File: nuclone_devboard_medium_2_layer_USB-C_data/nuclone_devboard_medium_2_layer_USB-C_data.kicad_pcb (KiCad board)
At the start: 2 copper layers, 50 x 76.2 mm, 40 parts, among them J1 JTAG_2X05, J2 TYPE-C-31-M-12, J3 nuclone_medium_left, J4 nuclone_medium_right, J5 Conn_02x06_Odd_Even, SW1 RESET, SW2 Bootloader, U1 MCP1702-3.3V, U2 TPESD0504C6

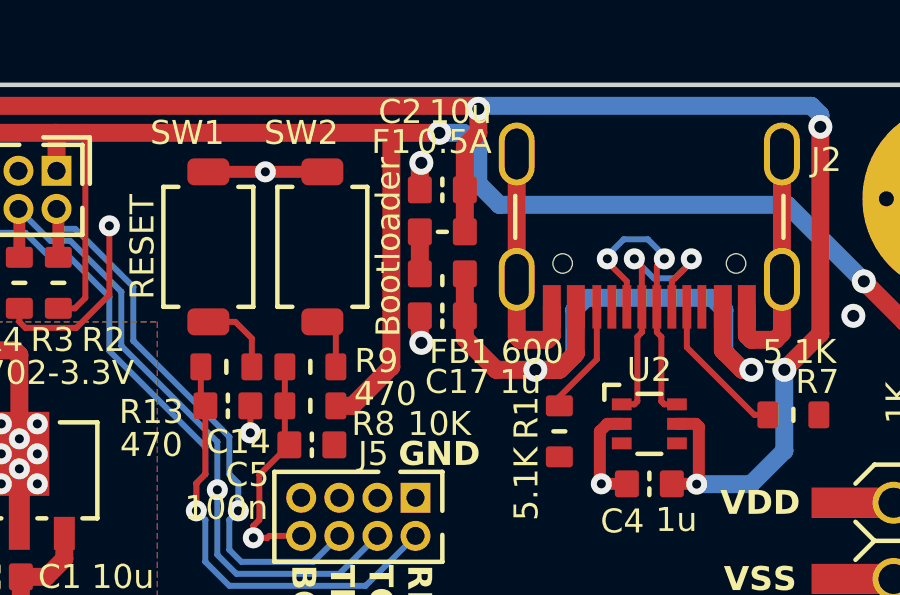
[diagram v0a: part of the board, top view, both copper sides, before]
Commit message: added diode, updated library
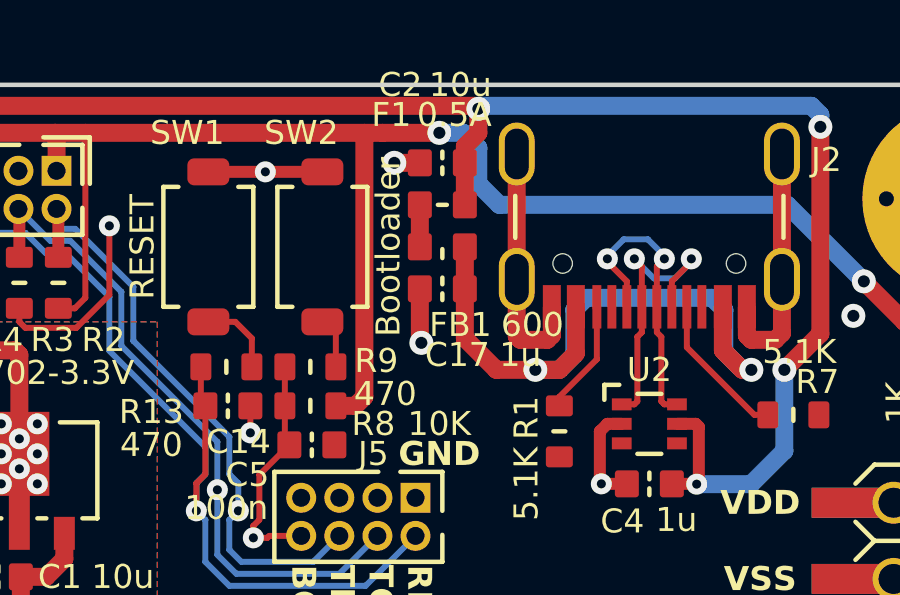
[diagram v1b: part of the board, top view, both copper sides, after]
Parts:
- moved C17 0.90 mm to (89.1, 67.8)
- moved F1 0.90 mm to (89.1, 65.0)
- moved C2 0.90 mm to (89.1, 63.6)
- moved FB1 0.90 mm to (89.1, 66.4)
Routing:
- net /VBUS: track 91.2 -> 90.3 mm
- net Net-(C17-Pad2): track 21.6 -> 22.5 mm
- net /VSS: track 44.6 -> 45.5 mm
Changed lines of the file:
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@@
   )
   (footprint "SquantorCapacitor:C_0603" (layer "F.Cu")
-    (at 89.1 64.5)
+    (at 89.1 63.6)
     (descr "Capacitor SMD 0603, reflow soldering, AVX (see smccp.pdf)")
     (tags "capacitor 0603")
@@
   )
   (footprint "SquantorFuse:F_0603_hand" (layer "F.Cu")
-    (at 89.1 65.9 180)
+    (at 89.1 65 180)
     (descr "Fuse SMD 0603, reflow soldering")
     (tags "fuse 0603")
@@
   )
   (footprint "SquantorInductor:L_0603" (layer "F.Cu")
-    (at 89.1 67.3)
+    (at 89.1 66.4)
     (descr "Inductor SMD 0603")
     (tags "Inductor 0402")
@@
   )
   (footprint "SquantorCapacitor:C_0603" (layer "F.Cu")
-    (at 89.1 68.7)
+    (at 89.1 67.8)
     (descr "Capacitor SMD 0603, reflow soldering, AVX (see smccp.pdf)")
     (tags "capacitor 0603")
@@
   (segment (start 67.8 63.6) (end 69.7 61.7) (width 0.6) (layer "F.Cu") (net 1))
   (segment (start 97.566774 74.3) (end 96.75 74.3) (width 0.4) (layer "F.Cu") (net 1))
-  (segment (start 90.3 62.6) (end 89.85 63.05) (width 0.6) (layer "F.Cu") (net 1))
-  (segment (start 89.85 64.5) (end 89.85 65.9) (width 0.6) (layer "F.Cu") (net 1))
   (segment (start 74.4 73.3) (end 75 73.8) (width 0.6) (layer "F.Cu") (net 1))
   (segment (start 101.7 69.3) (end 101.7 62.4) (width 0.6) (layer "F.Cu") (net 1))
   (segment (start 74.9 72.8) (end 75 72.8) (width 0.6) (layer "F.Cu") (net 1))
+  (segment (start 89.85 63.6) (end 89.85 65) (width 0.6) (layer "F.Cu") (net 1))
   (segment (start 75 72.9) (end 75 72.9) (width 0.6) (layer "F.Cu") (net 1))
   (segment (start 97.577735 74.310961) (end 97.65 74.238696) (width 0.4) (layer "F.Cu") (net 1))
-  (segment (start 90.3 61.8) (end 90.3 62.6) (width 0.6) (layer "F.Cu") (net 1))
   (segment (start 74.85 69.85) (end 75 70) (width 0.6) (layer "F.Cu") (net 1))
+  (segment (start 90.3 62.6) (end 89.85 63.05) (width 0.6) (layer "F.Cu") (net 1))
   (segment (start 69.7 69.85) (end 74.85 69.85) (width 0.6) (layer "F.Cu") (net 1))
   (segment (start 97.65 72.4) (end 97.55 72.3) (width 0.4) (layer "F.Cu") (net 1))
   (segment (start 75 70) (end 75 72.8) (width 0.6) (layer "F.Cu") (net 1))
-  (segment (start 89.85 63.05) (end 89.85 64.5) (width 0.6) (layer "F.Cu") (net 1))
+  (segment (start 90.3 61.8) (end 90.3 62.6) (width 0.6) (layer "F.Cu") (net 1))
   (segment (start 97.577735 74.310961) (end 97.566774 74.3) (width 0.4) (layer "F.Cu") (net 1))
   (segment (start 75 72.9) (end 74.4 73.3) (width 0.6) (layer "F.Cu") (net 1))
@@
   (segment (start 67.7 68.9) (end 67.8 68.8) (width 0.6) (layer "F.Cu") (net 1))
   (segment (start 69.7 68.9) (end 69.7 69.85) (width 0.6) (layer "F.Cu") (net 1))
+  (segment (start 89.85 63.05) (end 89.85 63.6) (width 0.6) (layer "F.Cu") (net 1))
   (segment (start 97.55 72.3) (end 96.92 72.3) (width 0.4) (layer "F.Cu") (net 1))
   (via (at 97.577735 74.310961) (size 0.7) (drill 0.3) (layers "F.Cu" "B.Cu") (net 1))
@@
   (segment (start 67.03 77.47) (end 66.04 77.47) (width 0.6) (layer "B.Cu") (net 1))
   (segment (start 67.1 77.4) (end 67.03 77.47) (width 0.6) (layer "B.Cu") (net 1))
-  (segment (start 88.35 67.3) (end 88.35 65.9) (width 0.6) (layer "F.Cu") (net 2))
+  (segment (start 88.35 66.4) (end 88.35 65) (width 0.6) (layer "F.Cu") (net 2))
   (segment (start 68.9 68.1) (end 70.2 68.1) (width 0.2) (layer "F.Cu") (net 3))
-  (segment (start 86.1 71.7) (end 85.55 71.7) (width 0.6) (layer "F.Cu") (net 3))
   (segment (start 76.5 76.8) (end 75.9 77.4) (width 0.6) (layer "F.Cu") (net 3))
   (segment (start 76.85 68.45) (end 77.2 68.1) (width 0.2) (layer "F.Cu") (net 3))
@@
   (segment (start 68.7 64) (end 70.1 62.6) (width 0.6) (layer "F.Cu") (net 3))
   (segment (start 68.7 67.9) (end 68.7 64) (width 0.6) (layer "F.Cu") (net 3))
+  (segment (start 86.5 62.6) (end 86.5 71.4) (width 0.6) (layer "F.Cu") (net 3))
   (segment (start 70.1 62.6) (end 76.2 62.6) (width 0.6) (layer "F.Cu") (net 3))
   (segment (start 108.97 74.93) (end 109 74.9) (width 0.6) (layer "F.Cu") (net 3))
@@
   (segment (start 68.7 67.9) (end 68.7 70.3) (width 0.6) (layer "F.Cu") (net 3))
   (segment (start 89 62.6) (end 87.1 62.6) (width 0.6) (layer "F.Cu") (net 3))
-  (segment (start 87.4 62.6) (end 87.4 70.4) (width 0.6) (layer "F.Cu") (net 3))
   (segment (start 76.24 62.64) (end 76.2 62.6) (width 0.6) (layer "F.Cu") (net 3))
   (segment (start 70.55 68.45) (end 71.1 68.45) (width 0.2) (layer "F.Cu") (net 3))
@@
   (segment (start 67.8 71.2) (end 67.8 74.93) (width 0.6) (layer "F.Cu") (net 3))
   (segment (start 75.05 78.35) (end 75 78.4) (width 0.6) (layer "F.Cu") (net 3))
-  (segment (start 87.4 70.4) (end 86.1 71.7) (width 0.6) (layer "F.Cu") (net 3))
   (segment (start 69.03 74.93) (end 67.12 74.93) (width 0.6) (layer "F.Cu") (net 3))
   (segment (start 108.9 68.9) (end 104.5 68.9) (width 0.6) (layer "F.Cu") (net 3))
+  (segment (start 86.5 71.4) (end 86.2 71.7) (width 0.6) (layer "F.Cu") (net 3))
+  (segment (start 86.2 71.7) (end 85.55 71.7) (width 0.6) (layer "F.Cu") (net 3))
   (segment (start 109 73.8) (end 109.2 73.6) (width 0.6) (layer "F.Cu") (net 3))
   (segment (start 75.05 77.4) (end 75.05 78.35) (width 0.6) (layer "F.Cu") (net 3))
@@
   (segment (start 92.6 69.5) (end 91.7 69.5) (width 0.6) (layer "F.Cu") (net 4))
   (segment (start 84.7 63.9) (end 83.2 63.9) (width 0.4) (layer "F.Cu") (net 4))
-  (segment (start 88.35 68.7) (end 88.35 69.55) (width 0.6) (layer "F.Cu") (net 4))
   (segment (start 94.4 74.3) (end 95.25 74.3) (width 0.4) (layer "F.Cu") (net 4))
-  (segment (start 88.35 69.55) (end 88.4 69.6) (width 0.6) (layer "F.Cu") (net 4))
   (segment (start 92.75 68.4) (end 92.75 69.35) (width 0.6) (layer "F.Cu") (net 4))
   (segment (start 100.2 69.5) (end 100.42 69.28) (width 0.6) (layer "F.Cu") (net 4))
@@
   (segment (start 75 68.9) (end 75.2 69.1) (width 0.2) (layer "F.Cu") (net 4))
   (segment (start 75.2 69.1) (end 76.9 69.1) (width 0.2) (layer "F.Cu") (net 4))
-  (segment (start 88.4 63.6) (end 88.35 63.65) (width 0.6) (layer "F.Cu") (net 4))
-  (segment (start 88.35 63.65) (end 88.35 64.5) (width 0.6) (layer "F.Cu") (net 4))
+  (segment (start 88.35 67.8) (end 88.35 69.55) (width 0.6) (layer "F.Cu") (net 4))
+  (segment (start 87.5 63.6) (end 88.35 63.6) (width 0.6) (layer "F.Cu") (net 4))
   (segment (start 100.42 63.305) (end 100.42 67.485) (width 0.6) (layer "F.Cu") (net 4))
   (segment (start 81.3 63.9) (end 83.2 63.9) (width 0.4) (layer "F.Cu") (net 4))
@@
   (segment (start 75 68.45) (end 75 68.9) (width 0.2) (layer "F.Cu") (net 4))
   (segment (start 76.9 69.1) (end 78 68) (width 0.2) (layer "F.Cu") (net 4))
+  (segment (start 88.35 69.55) (end 88.4 69.6) (width 0.6) (layer "F.Cu") (net 4))
   (segment (start 73.5 77.35) (end 73.55 77.4) (width 0.6) (layer "F.Cu") (net 4))
   (segment (start 91.58 69.38) (end 91.58 67.485) (width 0.6) (layer "F.Cu") (net 4))
@@
   (via (at 94.4 74.3) (size 0.7) (drill 0.3) (layers "F.Cu" "B.Cu") (net 4))
   (via (at 86.7 91) (size 0.7) (drill 0.3) (layers "F.Cu" "B.Cu") (free) (net 4))
-  (via (at 88.4 63.6) (size 0.8) (drill 0.4) (layers "F.Cu" "B.Cu") (net 4))
+  (via (at 87.5 63.6) (size 0.8) (drill 0.4) (layers "F.Cu" "B.Cu") (net 4))
   (via (at 66.6 61.8) (size 0.8) (drill 0.4) (layers "F.Cu" "B.Cu") (free) (net 4))
   (via (at 78 65.7) (size 0.7) (drill 0.3) (layers "F.Cu" "B.Cu") (net 4))
@@
   (segment (start 82.2 68.9) (end 82.75 69.45) (width 0.2) (layer "F.Cu") (net 19))
   (segment (start 92.2 70.5) (end 93 70.5) (width 0.6) (layer "F.Cu") (net 21))
-  (segment (start 92.2 70.5) (end 90.9 70.5) (width 0.6) (layer "F.Cu") (net 21))
-  (segment (start 89.85 68.7) (end 89.85 67.3) (width 0.6) (layer "F.Cu") (net 21))
+  (segment (start 90.9 70.5) (end 89.85 69.45) (width 0.6) (layer "F.Cu") (net 21))
   (segment (start 98.45 69.85) (end 98.45 68.4) (width 0.6) (layer "F.Cu") (net 21))
+  (segment (start 92.2 70.5) (end 90.9 70.5) (width 0.6) (layer "F.Cu") (net 21))
+  (segment (start 89.85 67.8) (end 89.85 66.4) (width 0.6) (layer "F.Cu") (net 21))
+  (segment (start 89.85 69.45) (end 89.85 67.8) (width 0.6) (layer "F.Cu") (net 21))
   (segment (start 93 70.5) (end 93.55 69.95) (width 0.6) (layer "F.Cu") (net 21))
   (segment (start 99.1 70.5) (end 98.45 69.85) (width 0.6) (layer "F.Cu") (net 21))
   (segment (start 99.4 70.5) (end 99.1 70.5) (width 0.6) (layer "F.Cu") (net 21))
-  (segment (start 89.85 69.45) (end 89.85 68.7) (width 0.6) (layer "F.Cu") (net 21))
   (segment (start 93.55 69.95) (end 93.55 68.4) (width 0.6) (layer "F.Cu") (net 21))
-  (segment (start 90.9 70.5) (end 89.85 69.45) (width 0.6) (layer "F.Cu") (net 21))
   (via (at 92.2 70.5) (size 0.8) (drill 0.4) (layers "F.Cu" "B.Cu") (net 21))
   (via (at 99.4 70.5) (size 0.8) (drill 0.4) (layers "F.Cu" "B.Cu") (net 21))

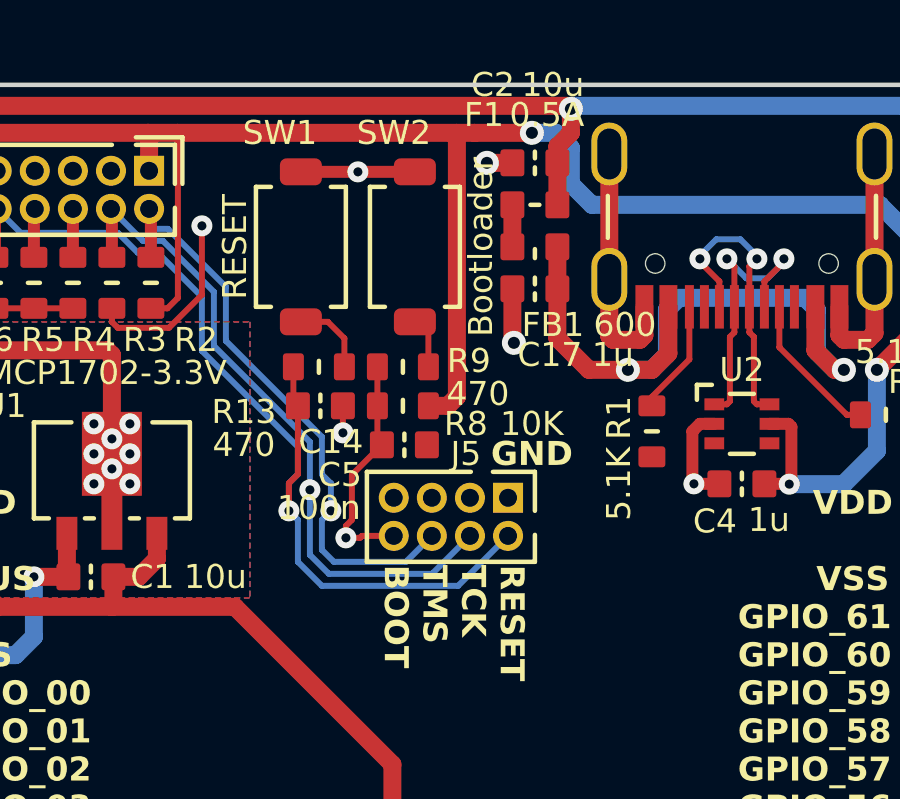
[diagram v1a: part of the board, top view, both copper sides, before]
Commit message: added diode in series
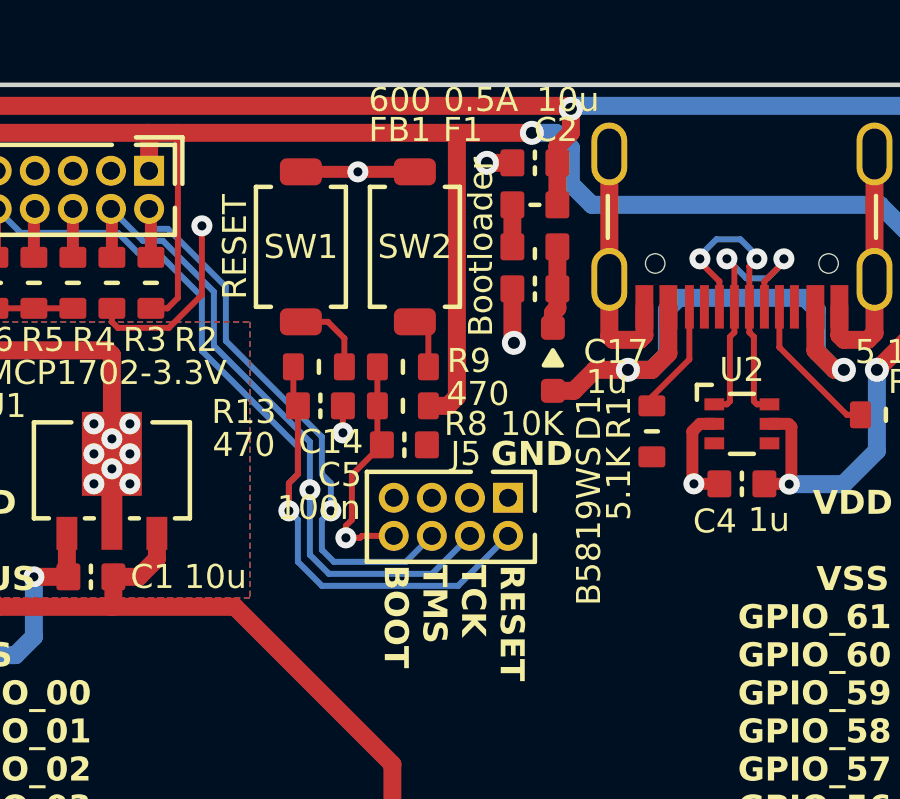
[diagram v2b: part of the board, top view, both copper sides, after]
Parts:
- added D1: B5819WS, SquantorDiodes:SOD-323-nexperia-hand, F.Cu at (89.7, 70.2)
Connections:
- net /Bootloader renamed /BOOT
- C17 pad 2: Net-(C17-Pad2) -> Net-(D1-K)
- FB1 pad 2: Net-(C17-Pad2) -> Net-(D1-K)
- J2 pad A4B9: Net-(C17-Pad2) -> Net-(D1-A)
- J2 pad B4A9: Net-(C17-Pad2) -> Net-(D1-A)
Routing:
- net Net-(C17-Pad2): track 22.5 -> 0.00 mm, vias 2 -> 0
- net Net-(D1-A): track 0.00 -> 19.5 mm, vias 0 -> 2
- net Net-(D1-K): track 0.00 -> 2.76 mm

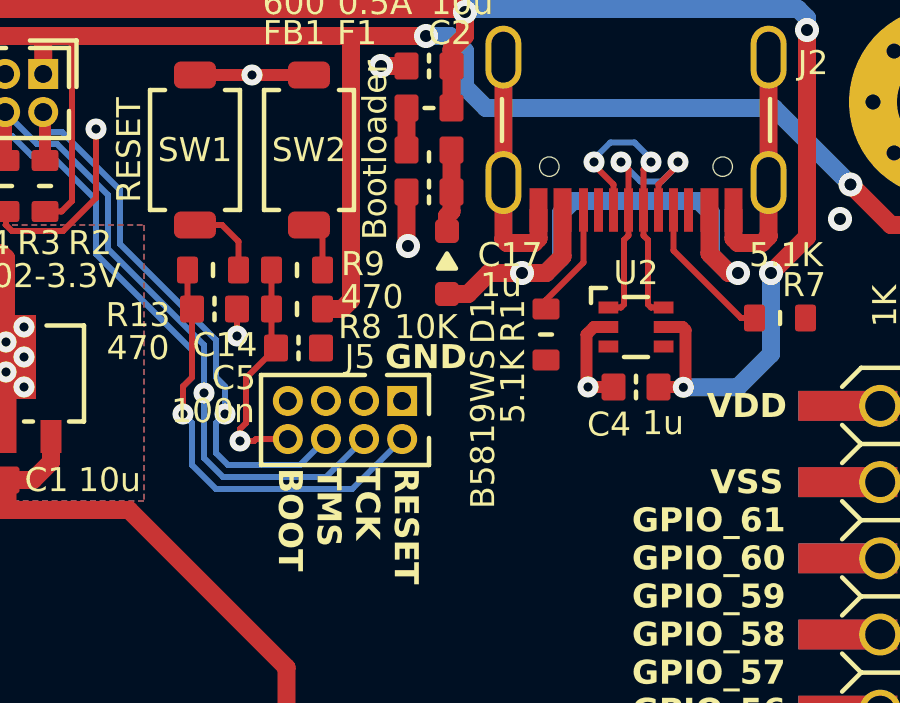
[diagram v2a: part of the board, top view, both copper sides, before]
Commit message: adjusted diode position a bit
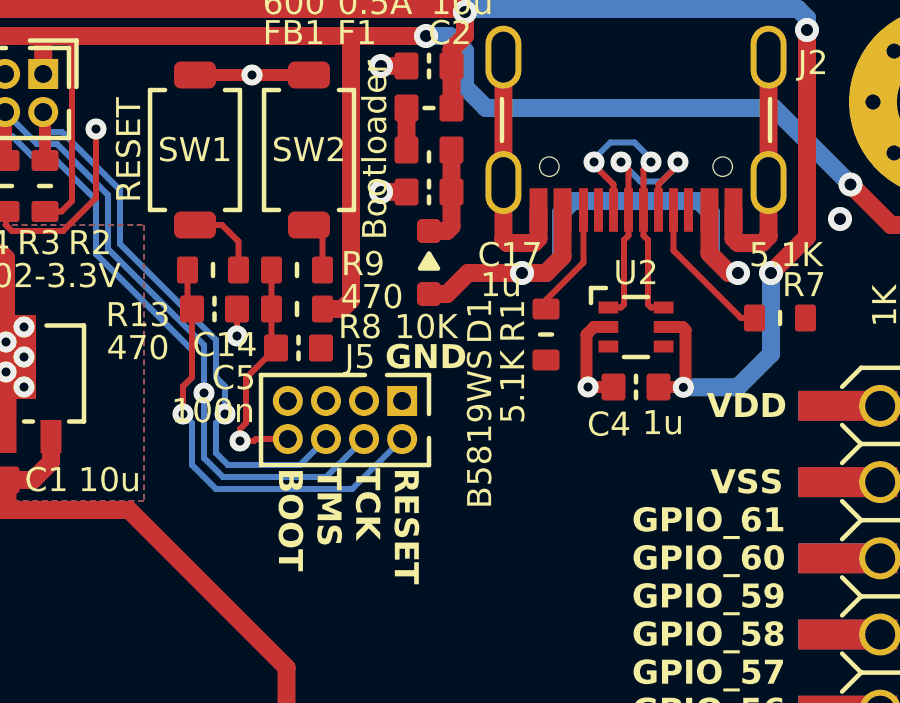
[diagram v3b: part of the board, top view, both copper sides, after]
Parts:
- moved D1 0.60 mm to (89.1, 70.2)
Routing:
- net /VSS: track 45.5 -> 44.5 mm
- net Net-(D1-K): track 2.76 -> 3.36 mm
- net Net-(D1-A): track 19.5 -> 20.1 mm
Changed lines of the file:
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@@
   )
   (footprint "SquantorDiodes:SOD-323-nexperia-hand" (layer "F.Cu")
-    (at 89.7 70.15 -90)
+    (at 89.1 70.15 -90)
     (descr "nexperia SOD-323 footprint hand soldering")
     (tags "SOD-323")
@@
     (property "ki_keywords" "diode")
     (attr smd)
-    (fp_text reference "D1" (at 1.95 -1.2 90 unlocked) (layer "F.SilkS")
-        (effects (font (size 0.8 0.8) (thickness 0.15)))
-    )
-    (fp_text value "B5819WS" (at 5.55 -1.2 90 unlocked) (layer "F.SilkS")
+    (fp_text reference "D1" (at 1.95 -1.7 90 unlocked) (layer "F.SilkS")
+        (effects (font (size 0.8 0.8) (thickness 0.15)))
+    )
+    (fp_text value "B5819WS" (at 5.55 -1.7 90 unlocked) (layer "F.SilkS")
         (effects (font (size 0.8 0.8) (thickness 0.15)))
     )
@@
   (segment (start 73.5 75.95) (end 73.5 77.35) (width 0.6) (layer "F.Cu") (net 4))
   (segment (start 91.7 69.5) (end 91.58 69.38) (width 0.6) (layer "F.Cu") (net 4))
+  (segment (start 87.5 67.8) (end 88.35 67.8) (width 0.6) (layer "F.Cu") (net 4))
   (segment (start 75 68.9) (end 75.2 69.1) (width 0.2) (layer "F.Cu") (net 4))
   (segment (start 75.2 69.1) (end 76.9 69.1) (width 0.2) (layer "F.Cu") (net 4))
-  (segment (start 88.35 67.8) (end 88.35 69.55) (width 0.6) (layer "F.Cu") (net 4))
   (segment (start 87.5 63.6) (end 88.35 63.6) (width 0.6) (layer "F.Cu") (net 4))
   (segment (start 100.42 63.305) (end 100.42 67.485) (width 0.6) (layer "F.Cu") (net 4))
@@
   (segment (start 75 68.45) (end 75 68.9) (width 0.2) (layer "F.Cu") (net 4))
   (segment (start 76.9 69.1) (end 78 68) (width 0.2) (layer "F.Cu") (net 4))
-  (segment (start 88.35 69.55) (end 88.4 69.6) (width 0.6) (layer "F.Cu") (net 4))
   (segment (start 73.5 77.35) (end 73.55 77.4) (width 0.6) (layer "F.Cu") (net 4))
   (segment (start 91.58 69.38) (end 91.58 67.485) (width 0.6) (layer "F.Cu") (net 4))
@@
   (via (at 78 65.7) (size 0.7) (drill 0.3) (layers "F.Cu" "B.Cu") (net 4))
   (via (at 82.7 72.6) (size 0.7) (drill 0.3) (layers "F.Cu" "B.Cu") (net 4))
-  (via (at 88.4 69.6) (size 0.8) (drill 0.4) (layers "F.Cu" "B.Cu") (net 4))
+  (via (at 87.5 67.8) (size 0.8) (drill 0.4) (layers "F.Cu" "B.Cu") (net 4))
   (via (at 72.4 77.4) (size 0.7) (drill 0.3) (layers "F.Cu" "B.Cu") (net 4))
   (segment (start 72.4 79.4) (end 72.4 77.4) (width 0.6) (layer "B.Cu") (net 4))
@@
   (segment (start 94.25 68.4) (end 94.2 68.45) (width 0.2) (layer "F.Cu") (net 24))
   (segment (start 94.25 70.15) (end 93 71.4) (width 0.2) (layer "F.Cu") (net 24))
-  (segment (start 89.85 67.8) (end 89.85 68.45) (width 0.6) (layer "F.Cu") (net 26))
+  (segment (start 89.85 68.95) (end 89.7 69.1) (width 0.6) (layer "F.Cu") (net 26))
+  (segment (start 89.7 69.1) (end 89.1 69.1) (width 0.6) (layer "F.Cu") (net 26))
   (segment (start 89.85 67.8) (end 89.85 66.4) (width 0.6) (layer "F.Cu") (net 26))
-  (segment (start 89.85 68.45) (end 89.7 68.6) (width 0.6) (layer "F.Cu") (net 26))
-  (segment (start 89.7 68.6) (end 89.7 69.1) (width 0.6) (layer "F.Cu") (net 26))
+  (segment (start 89.85 67.8) (end 89.85 68.95) (width 0.6) (layer "F.Cu") (net 26))
   (segment (start 95.75 68.4) (end 95.75 67.05) (width 0.2) (layer "F.Cu") (net 81))
   (segment (start 95.6 71.55) (end 95.5 71.65) (width 0.2) (layer "F.Cu") (net 81))
@@
   (segment (start 85.1 68.9) (end 85.5 68.9) (width 0.2) (layer "F.Cu") (net 85))
   (segment (start 85.55 68.95) (end 85.55 70.4) (width 0.2) (layer "F.Cu") (net 85))
+  (segment (start 92.2 70.5) (end 90.4 70.5) (width 0.6) (layer "F.Cu") (net 86))
   (segment (start 92.2 70.5) (end 93 70.5) (width 0.6) (layer "F.Cu") (net 86))
+  (segment (start 89.7 71.2) (end 89.1 71.2) (width 0.6) (layer "F.Cu") (net 86))
+  (segment (start 90.4 70.5) (end 89.7 71.2) (width 0.6) (layer "F.Cu") (net 86))
   (segment (start 98.45 69.85) (end 98.45 68.4) (width 0.6) (layer "F.Cu") (net 86))
   (segment (start 93 70.5) (end 93.55 69.95) (width 0.6) (layer "F.Cu") (net 86))
   (segment (start 99.1 70.5) (end 98.45 69.85) (width 0.6) (layer "F.Cu") (net 86))
   (segment (start 99.4 70.5) (end 99.1 70.5) (width 0.6) (layer "F.Cu") (net 86))
-  (segment (start 90.4 71.2) (end 89.7 71.2) (width 0.6) (layer "F.Cu") (net 86))
-  (segment (start 91.1 70.5) (end 90.4 71.2) (width 0.6) (layer "F.Cu") (net 86))
   (segment (start 93.55 69.95) (end 93.55 68.4) (width 0.6) (layer "F.Cu") (net 86))
-  (segment (start 92.2 70.5) (end 91.1 70.5) (width 0.6) (layer "F.Cu") (net 86))
   (via (at 92.2 70.5) (size 0.8) (drill 0.4) (layers "F.Cu" "B.Cu") (net 86))
   (via (at 99.4 70.5) (size 0.8) (drill 0.4) (layers "F.Cu" "B.Cu") (net 86))
